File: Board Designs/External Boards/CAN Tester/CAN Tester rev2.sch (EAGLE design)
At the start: 27 parts, among them M1 Minifit, M2 Nanofit, M3 Nanofit-1, M4 Minifit-1, U1 ISOLATED CAN TRANSCIEVER, U3 TEENSY_3.2_SIMPLE, U4 CHARACTER_LCD

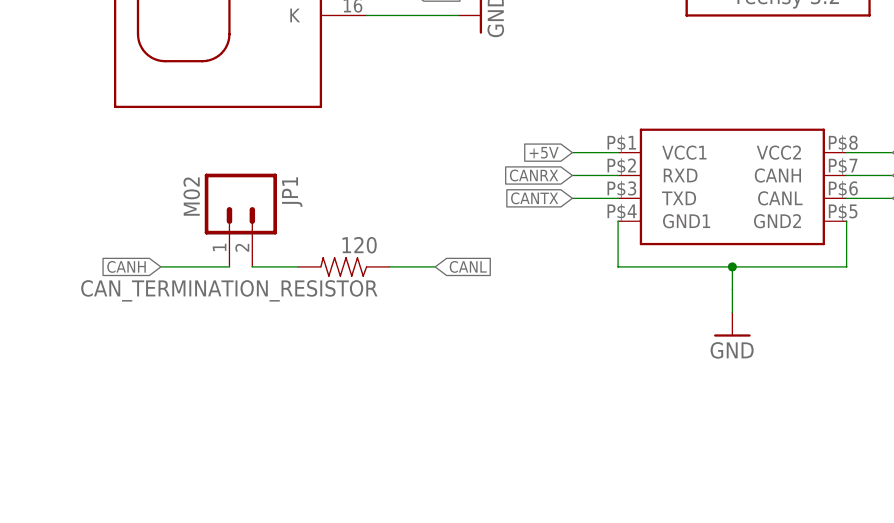
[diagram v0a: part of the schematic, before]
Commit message: Began work on Rev 2 of CAN_Tester, fixing the existing issues with the Rev 1 board but not isolating the isocan yet.
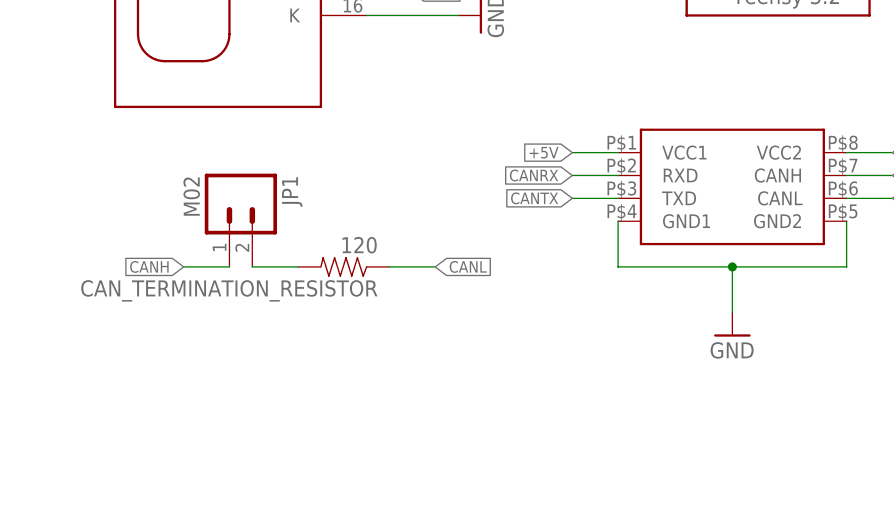
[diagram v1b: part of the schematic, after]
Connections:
- removed net N$16: U1.GND1, U1.GND2
- new net N$15: CAN_TERMINATION_RESISTOR.2, JP1.2
- net CANL: no longer CAN_TERMINATION_RESISTOR.2, JP1.2
- net GND: now also U1.GND1, U1.GND2
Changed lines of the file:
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@@
 <?xml version="1.0" encoding="utf-8"?>
 <!DOCTYPE eagle SYSTEM "eagle.dtd">
-<eagle version="9.2.1">
+<eagle version="9.2.2">
 <drawing>
 <settings>
@@
 </segment>
 <segment>
-<pinref part="CAN_TERMINATION_RESISTOR" gate="G$1" pin="1"/>
-<pinref part="CAN_TERMINATION_RESISTOR" gate="G$1" pin="2"/>
-<wire x1="53.34" y1="0" x2="48.26" y2="0" width="0.1524" layer="91"/>
-<wire x1="63.5" y1="0" x2="68.58" y2="0" width="0.1524" layer="91"/>
-<label x="68.58" y="0" size="1.27" layer="95" xref="yes"/>
-<pinref part="JP1" gate="G$1" pin="2"/>
-</segment>
-<segment>
 <pinref part="M3" gate="-3" pin="S"/>
 <wire x1="139.7" y1="93.98" x2="132.08" y2="93.98" width="0.1524" layer="91"/>
@@
 <wire x1="139.7" y1="81.28" x2="132.08" y2="81.28" width="0.1524" layer="91"/>
 <label x="132.08" y="81.28" size="1.27" layer="95" rot="R180" xref="yes"/>
+</segment>
+<segment>
+<pinref part="CAN_TERMINATION_RESISTOR" gate="G$1" pin="1"/>
+<wire x1="63.5" y1="0" x2="68.58" y2="0" width="0.1524" layer="91"/>
+<label x="68.58" y="0" size="1.27" layer="95" xref="yes"/>
 </segment>
 </net>
@@
 <segment>
 <pinref part="GND5" gate="1" pin="GND"/>
-<wire x1="101.6" y1="-5.08" x2="101.6" y2="-2.54" width="0.1524" layer="91"/>
+<pinref part="U1" gate="G$1" pin="GND2"/>
+<wire x1="114.3" y1="5.08" x2="114.3" y2="0" width="0.1524" layer="91"/>
+<pinref part="U1" gate="G$1" pin="GND1"/>
+<wire x1="88.9" y1="5.08" x2="88.9" y2="0" width="0.1524" layer="91"/>
+<wire x1="88.9" y1="0" x2="101.6" y2="0" width="0.1524" layer="91"/>
+<wire x1="101.6" y1="0" x2="101.6" y2="-5.08" width="0.1524" layer="91"/>
+<wire x1="114.3" y1="0" x2="101.6" y2="0" width="0.1524" layer="91"/>
+<junction x="101.6" y="0"/>
 </segment>
 <segment>
@@
 </segment>
 <segment>
-<wire x1="45.72" y1="0" x2="38.1" y2="0" width="0.1524" layer="91"/>
-<label x="38.1" y="0" size="1.27" layer="95" rot="R180" xref="yes"/>
-<pinref part="JP1" gate="G$1" pin="1"/>
-</segment>
-<segment>
 <pinref part="M2" gate="-4" pin="S"/>
 <wire x1="109.22" y1="91.44" x2="101.6" y2="91.44" width="0.1524" layer="91"/>
@@
 <wire x1="139.7" y1="78.74" x2="132.08" y2="78.74" width="0.1524" layer="91"/>
 <label x="132.08" y="78.74" size="1.27" layer="95" rot="R180" xref="yes"/>
+</segment>
+<segment>
+<pinref part="JP1" gate="G$1" pin="1"/>
+<wire x1="45.72" y1="0" x2="40.64" y2="0" width="0.1524" layer="91"/>
+<label x="40.64" y="0" size="1.27" layer="95" rot="R180" xref="yes"/>
 </segment>
 </net>
@@
 </segment>
 </net>
-<net name="N$16" class="0">
-<segment>
-<pinref part="U1" gate="G$1" pin="GND2"/>
-<wire x1="114.3" y1="5.08" x2="114.3" y2="0" width="0.1524" layer="91"/>
-<pinref part="U1" gate="G$1" pin="GND1"/>
-<wire x1="88.9" y1="5.08" x2="88.9" y2="0" width="0.1524" layer="91"/>
-<wire x1="88.9" y1="0" x2="101.6" y2="0" width="0.1524" layer="91"/>
-<wire x1="101.6" y1="0" x2="101.6" y2="-2.54" width="0.1524" layer="91"/>
-<wire x1="114.3" y1="0" x2="101.6" y2="0" width="0.1524" layer="91"/>
-<junction x="101.6" y="0"/>
-</segment>
-</net>
 <net name="VO" class="0">
 <segment>
@@
 </segment>
 </net>
+<net name="N$15" class="0">
+<segment>
+<pinref part="CAN_TERMINATION_RESISTOR" gate="G$1" pin="2"/>
+<pinref part="JP1" gate="G$1" pin="2"/>
+<wire x1="53.34" y1="0" x2="48.26" y2="0" width="0.1524" layer="91"/>
+</segment>
+</net>

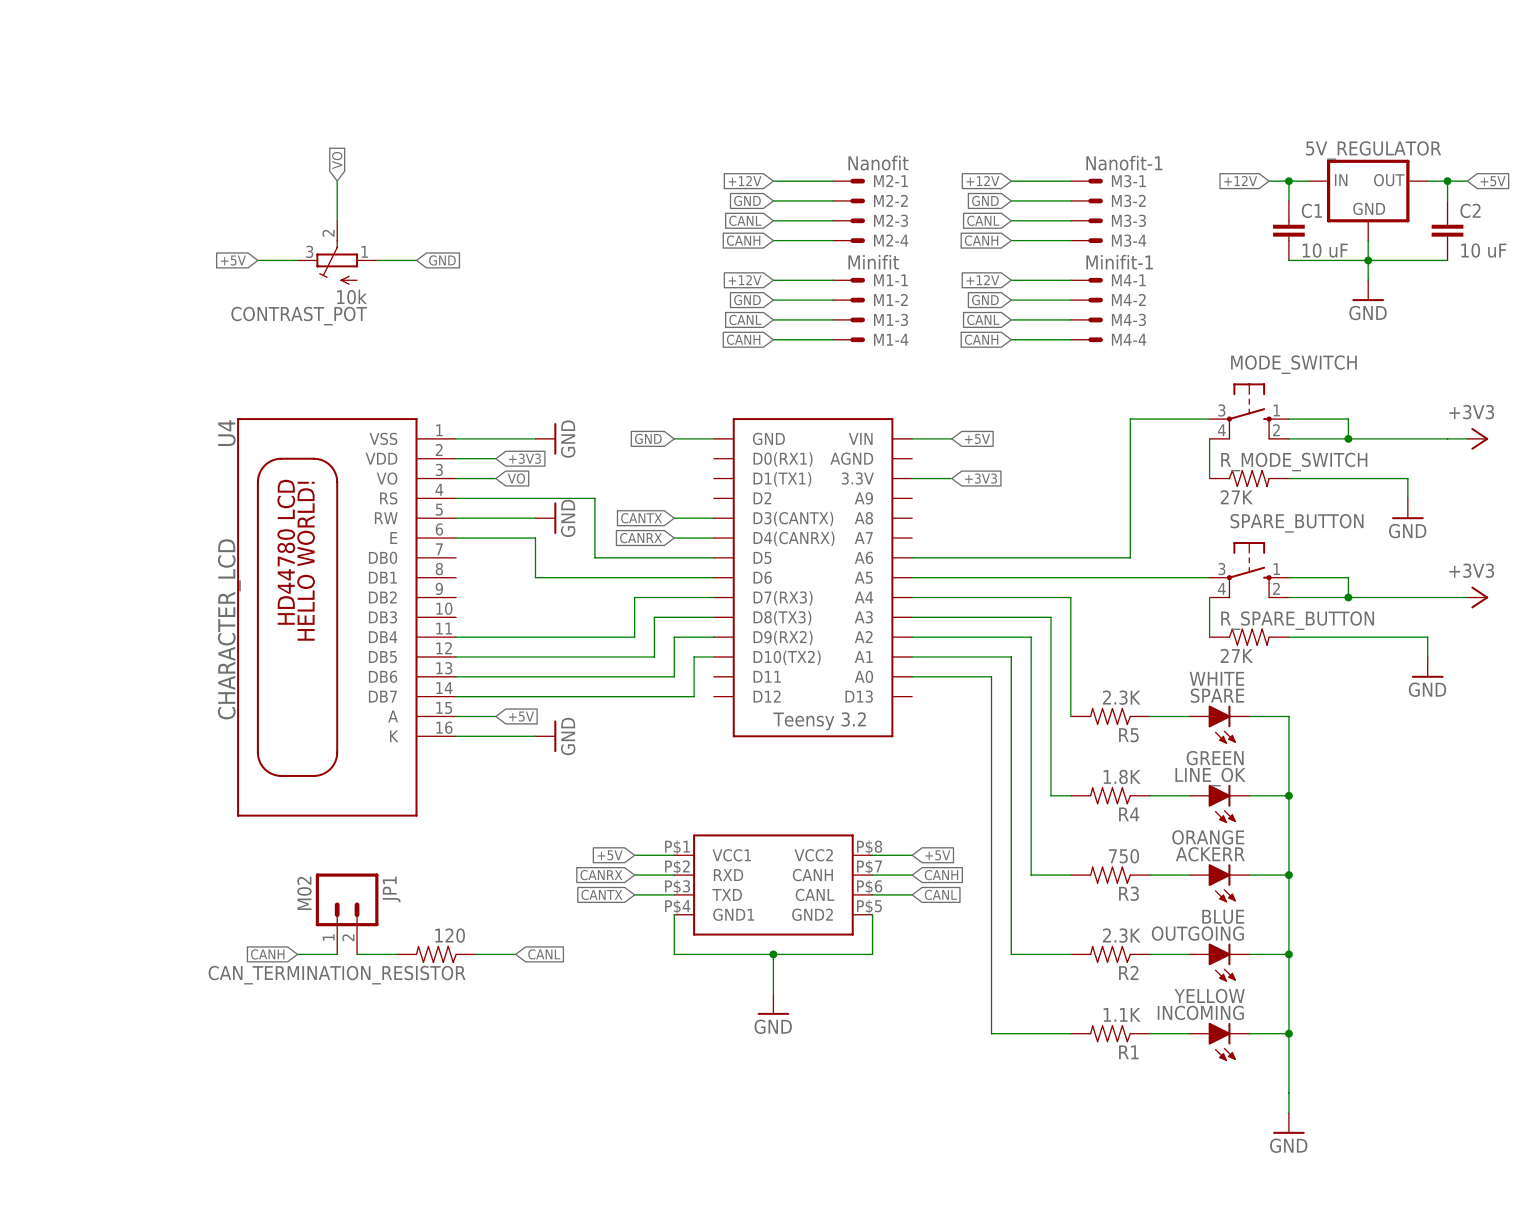
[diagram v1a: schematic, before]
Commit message: Updated with true isolation for separate 5V for the isocan and teensy
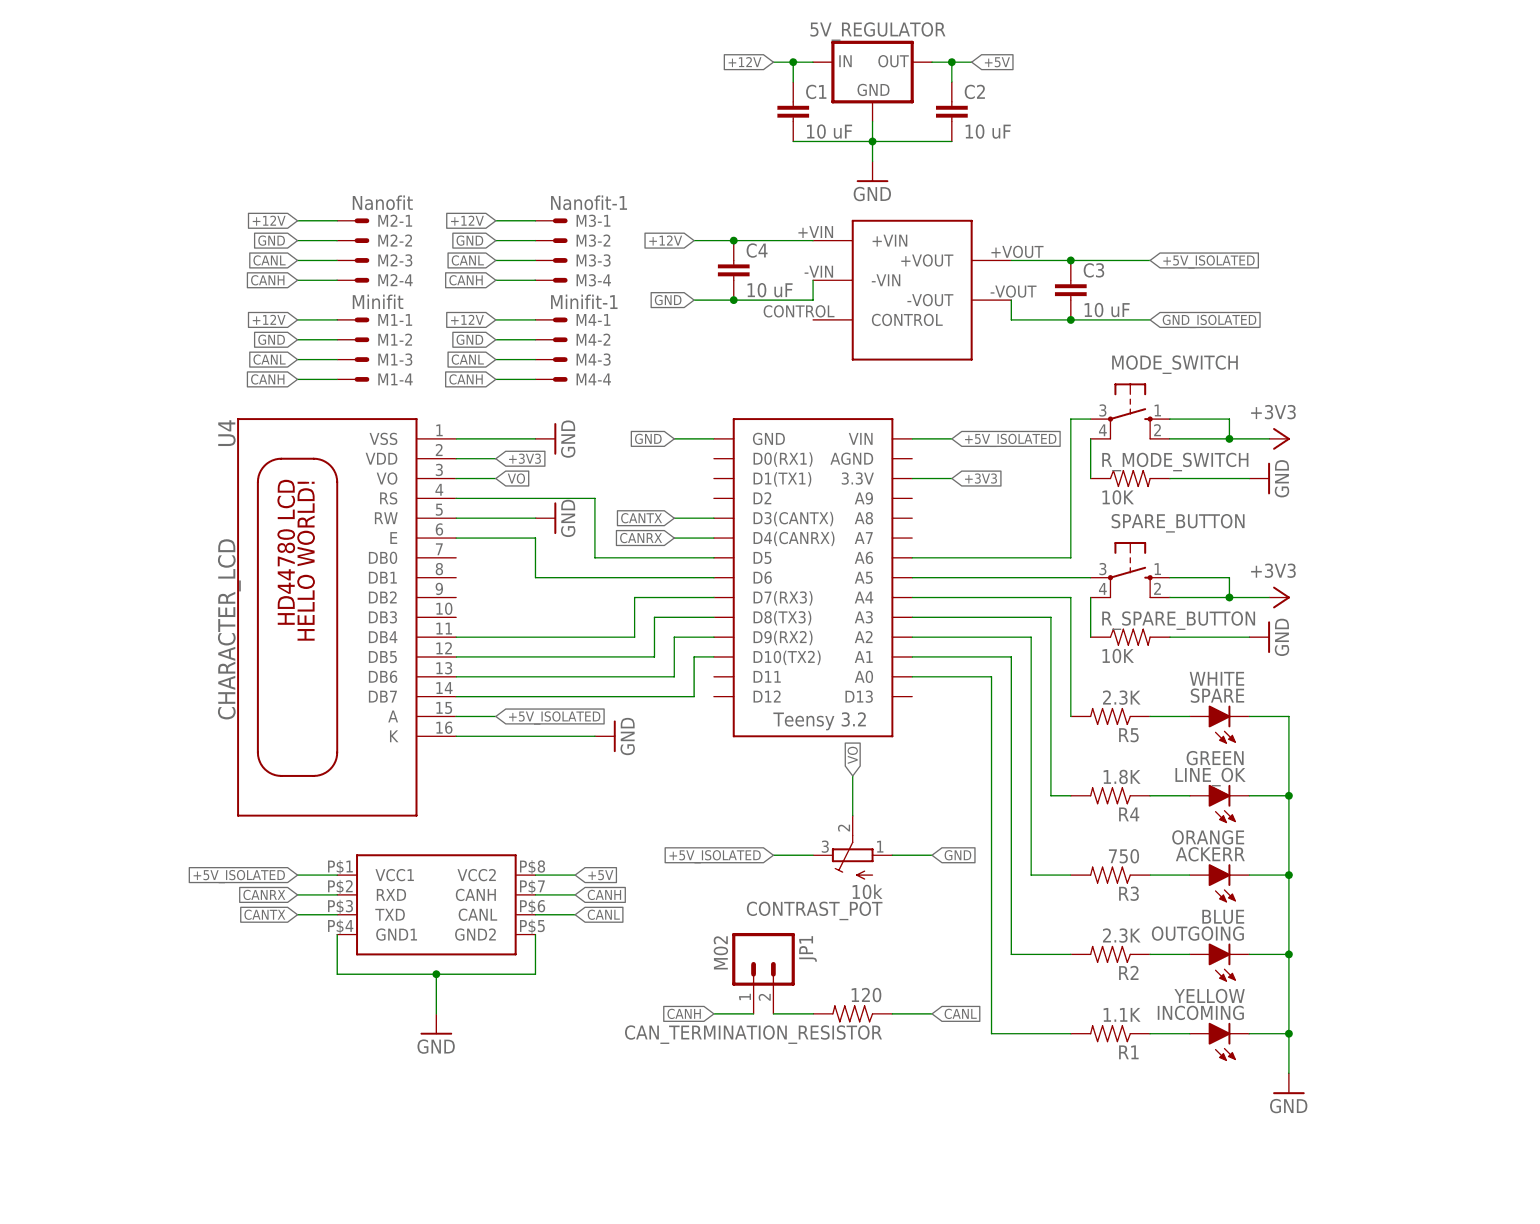
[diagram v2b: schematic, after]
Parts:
- added C3, C4: 10 uF, HyTechDevices:CAP0805
- added U$1: NCS1S1205SC-12V-5VCONVERTER, HyTechDevices:NCS1S1205SC-12V-5VCONVERTER
- R_MODE_SWITCH, R_SPARE_BUTTON: value 27K -> 10K
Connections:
- new net +5V_ISOLATED: C3.1, CONTRAST_POT.E, U$1.+VOUT, U1.VCC1, U3.VIN, U4.A
- new net GND_ISOLATED: C3.2, U$1.-VOUT
- net +12V: now also C4.1, U$1.+VIN
- net +5V: no longer CONTRAST_POT.E, U1.VCC1, U3.VIN, U4.A
- net GND: now also C4.2, U$1.-VIN
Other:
- moved on the sheet: 5V_REGULATOR, C1, C2, CAN_TERMINATION_RESISTOR, CONTRAST_POT, JP1, M1-1, M1-2, M1-3, M1-4, M2-1, M2-2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

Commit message: Finished isolating and started work on fixing CAN_Tester board
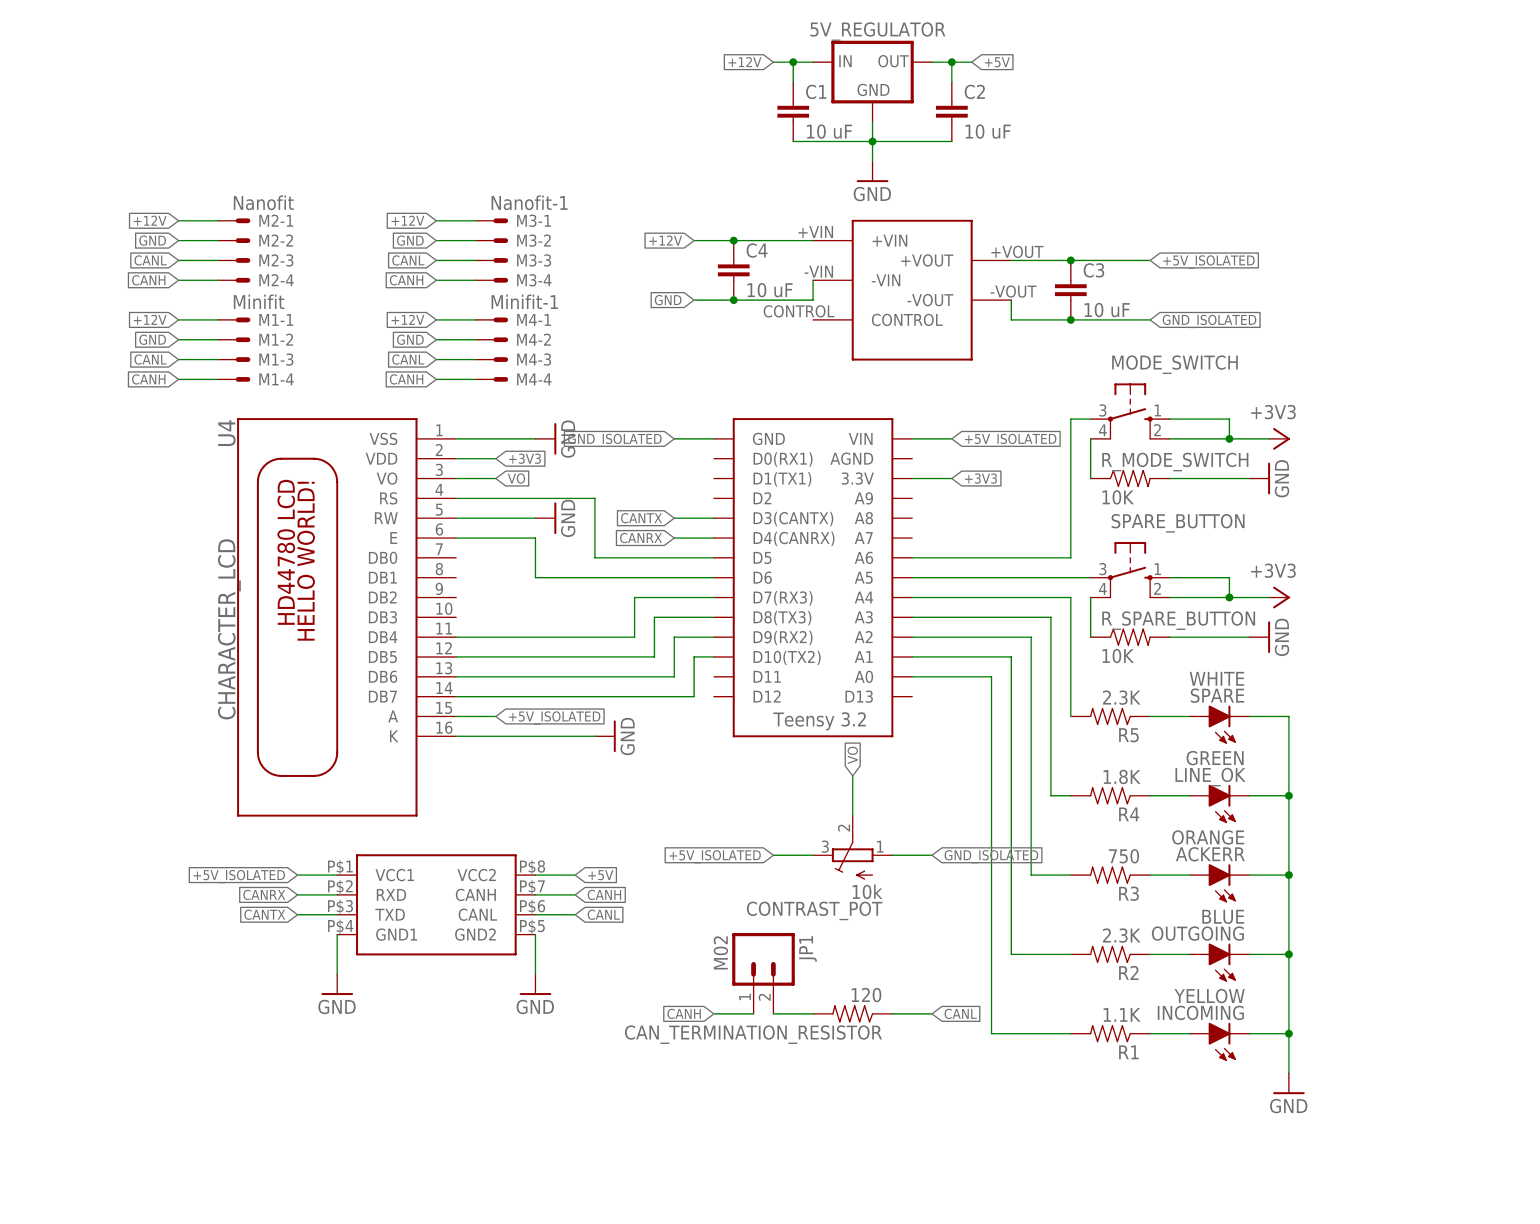
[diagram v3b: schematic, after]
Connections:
- net GND: no longer ACKERR.C, CONTRAST_POT.A, INCOMING.C, LINE_OK.C, OUTGOING.C, R_MODE_SWITCH.2, R_SPARE_BUTTON.2, SPARE.C, U1.GND1, U3.GND, U4.K, U4.RW, U4.VSS
- net GND_ISOLATED: now also ACKERR.C, CONTRAST_POT.A, INCOMING.C, LINE_OK.C, OUTGOING.C, R_MODE_SWITCH.2, R_SPARE_BUTTON.2, SPARE.C, U1.GND1, U3.GND, U4.K, U4.RW, U4.VSS
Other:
- moved on the sheet: M1-1, M1-2, M1-3, M1-4, M2-1, M2-2, M2-3, M2-4, M3-1, M3-2, M3-3, M3-4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

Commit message: Fixed circuit to have true isolation in CAN_Tester, and started work on new board layout
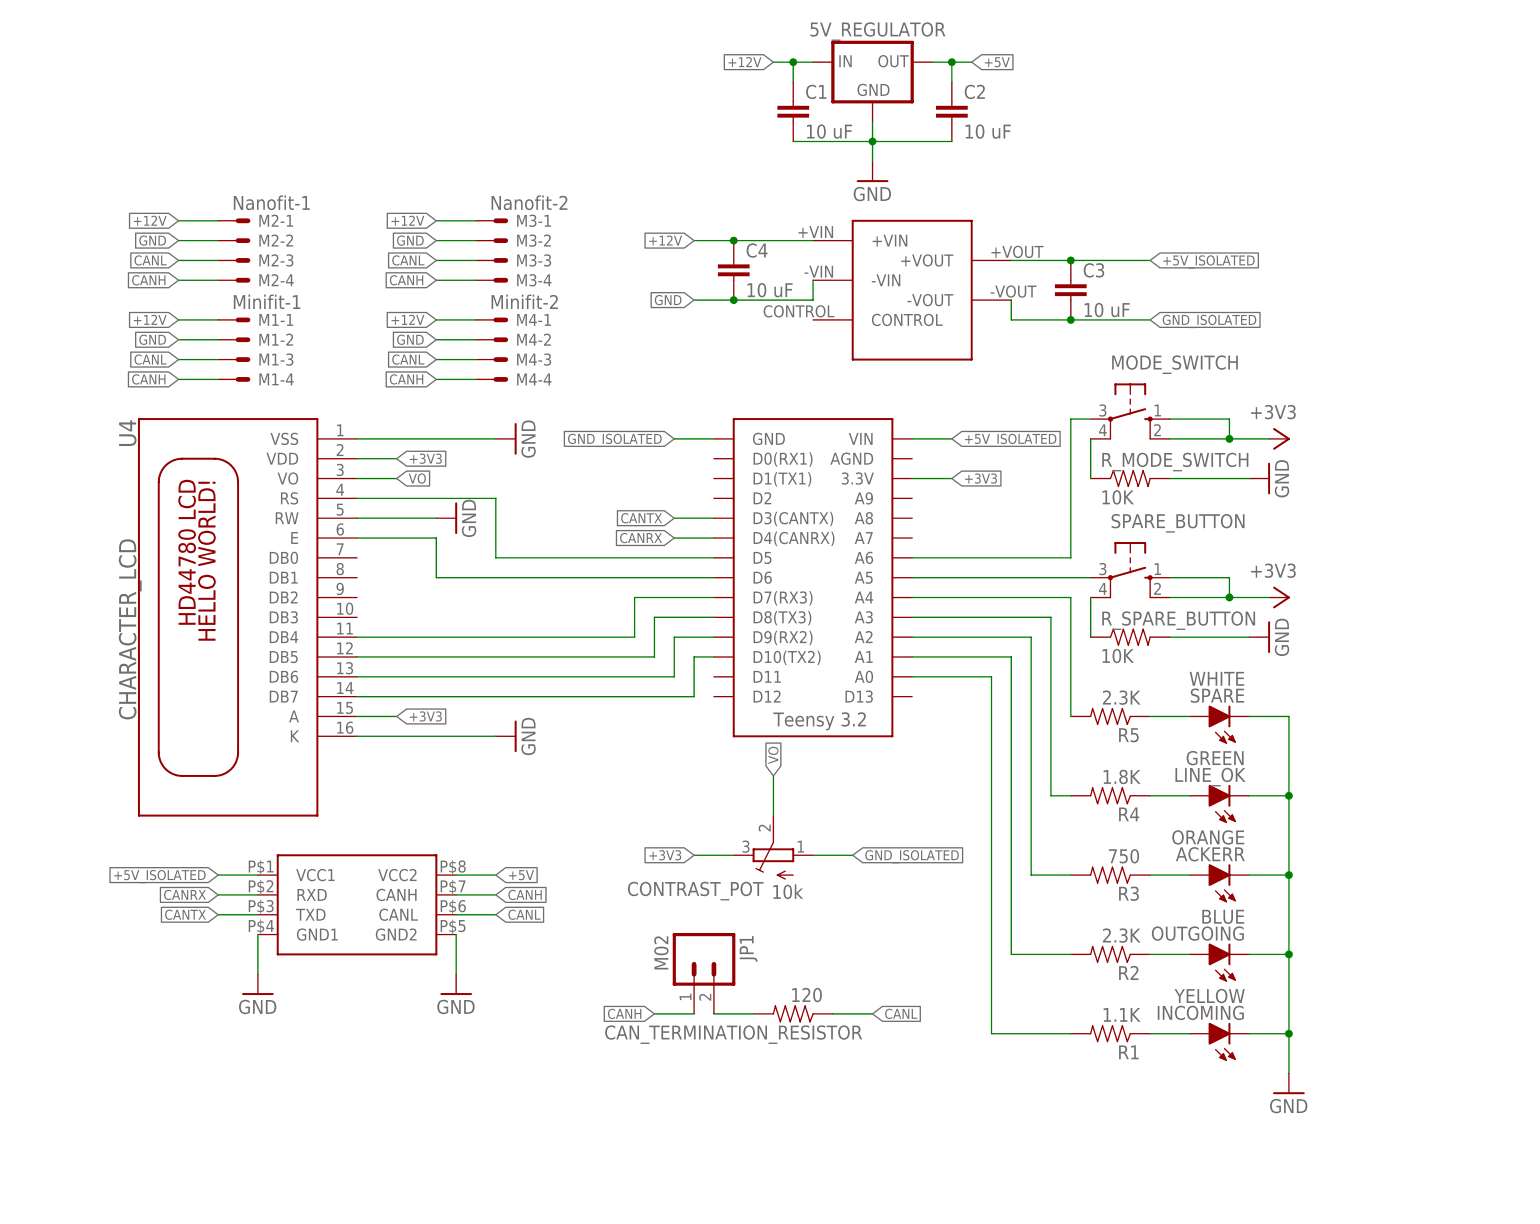
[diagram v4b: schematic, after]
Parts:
- M1: value Minifit -> Minifit-1
- M2: value Nanofit -> Nanofit-1
- M3: value Nanofit-1 -> Nanofit-2
- M4: value Minifit-1 -> Minifit-2
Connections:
- net +3V3: now also CONTRAST_POT.E, U4.A
- net +5V_ISOLATED: no longer CONTRAST_POT.E, U4.A
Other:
- moved on the sheet: CAN_TERMINATION_RESISTOR, CONTRAST_POT, JP1, U4
